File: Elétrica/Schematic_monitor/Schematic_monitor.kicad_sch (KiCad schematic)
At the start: 49 parts, among them J1 Conn_01x04, J2 USB_B_Micro, J3 Eletrode 1, J4 Eletrode 2, SW1 SW_Push, SW2 SW_SPDT, U1 STM32F446RET6TR, U2 LM1117S-3.3, U3 MLX90614ESF-ACC-000-TU, U4 MAX30100EFD+, U5 AD623, U6 LM358, U7 LM358, U8 LM358, Y1 Crystal_25MHz

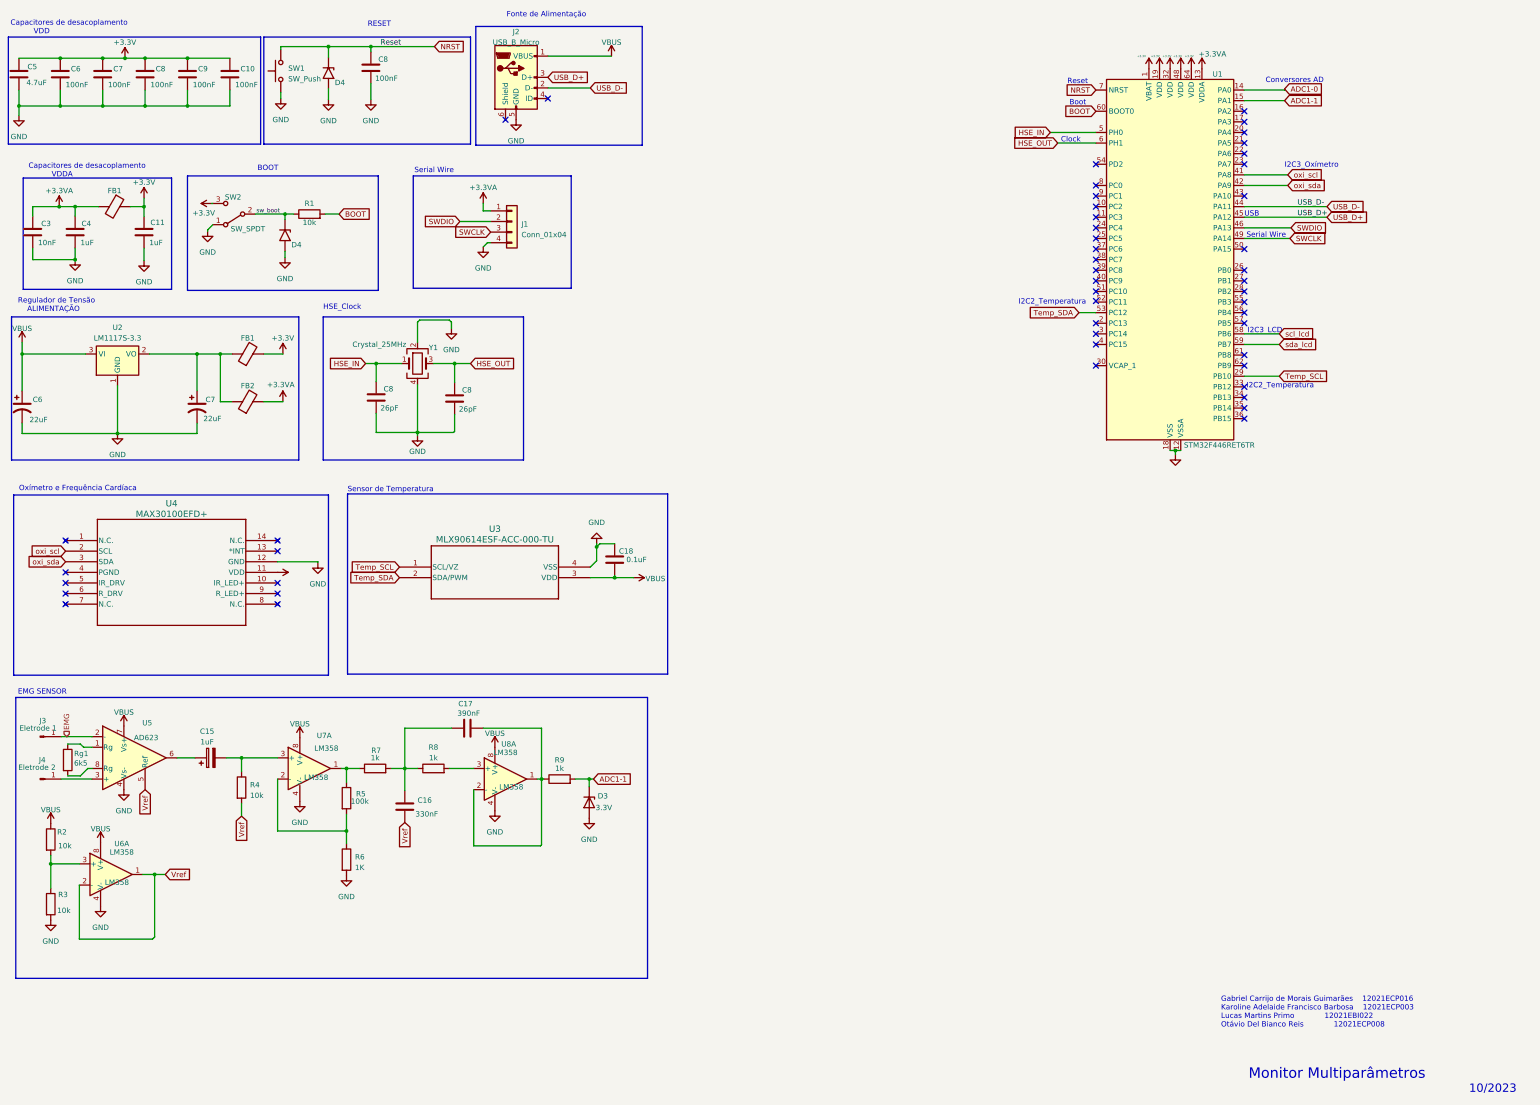
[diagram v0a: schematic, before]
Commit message: Versão PRJ2 e PRJ3 quase finalizada
Poucos detalhes precisam ser alterados para o envio dos trabalhos pelo menos do PRJ2. PRJ3 está finalizado
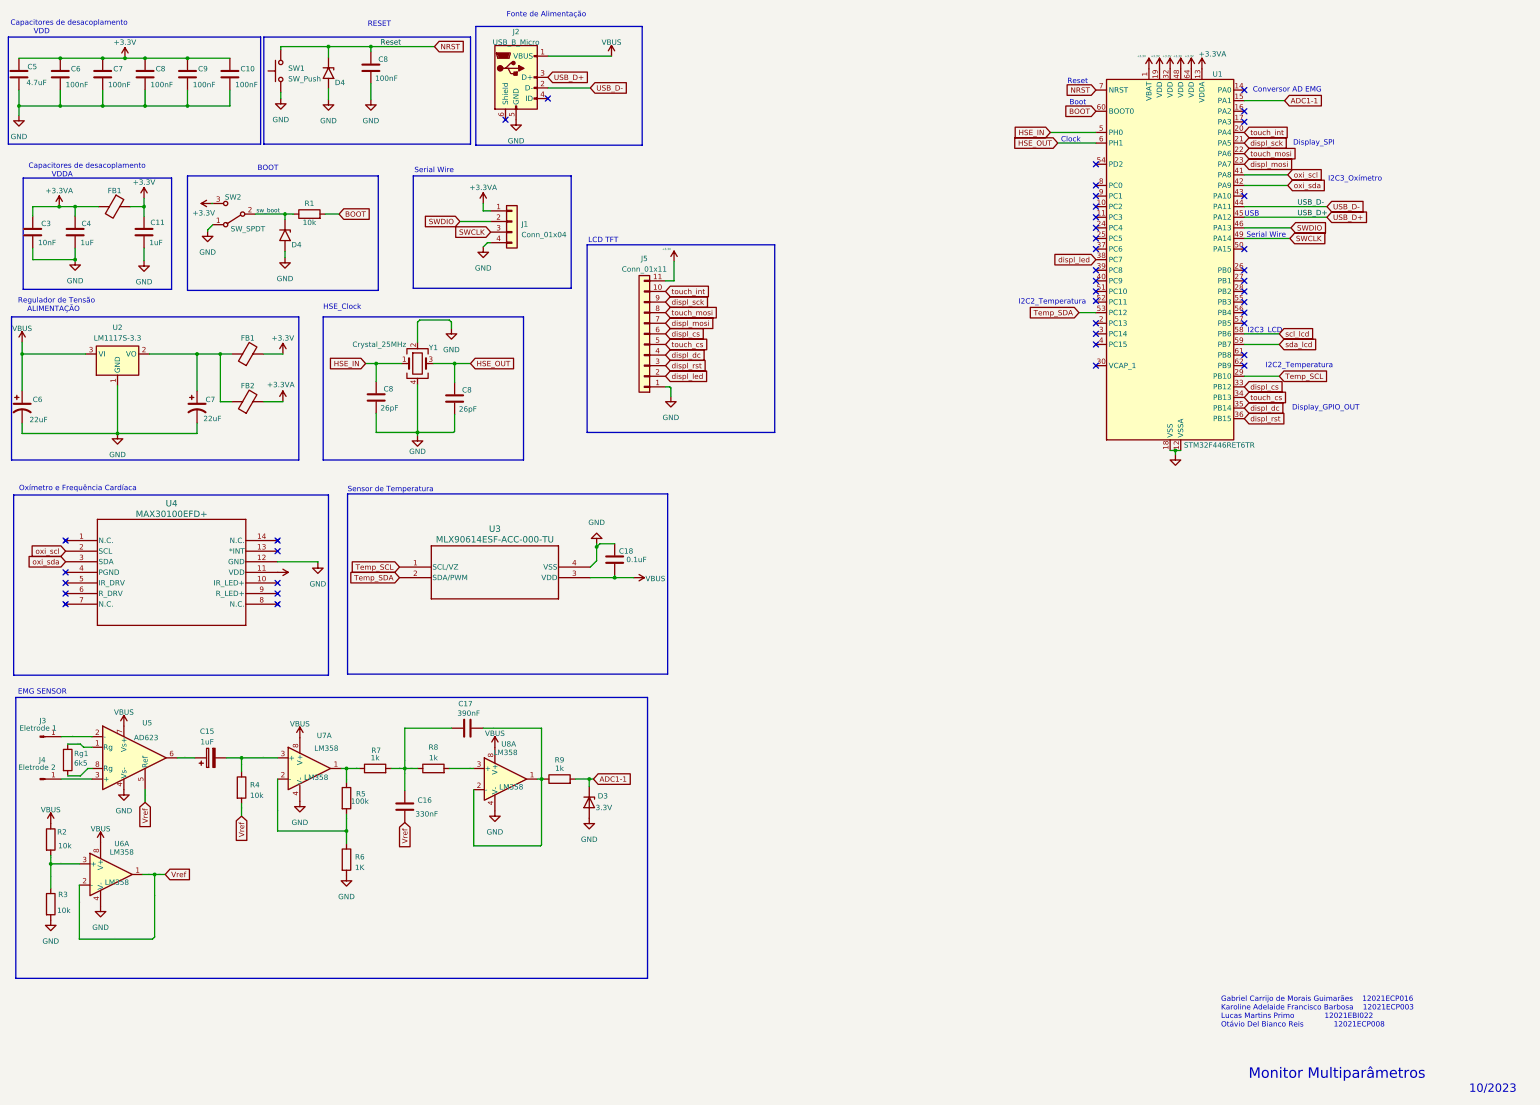
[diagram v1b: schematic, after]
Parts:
- added J5: Conn_01x11, Connector_PinSocket_1.00mm:PinSocket_1x11_P1.00mm_Vertical_SMD_Pin1Right, symbol Connector_Generic:Conn_01x11
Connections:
- net EMG is gone; now on net ADC1-1: J3.1 (Pin_1), U5.2 (-)
- net Vref is gone; now on net ADC1-1: C16.2, R4.2, U5.5 (Ref), U6.1, U6.2 (-)
- net +3.3V: now also J5.11 (Pin_11)
- net ADC1-1: now also C15.1, C15.2, C16.1, C17.1, C17.2, J4.1 (Pin_1), R2.2, R3.1, R4.1, R5.1, R5.2, R6.1, R7.1, R7.2, R8.1, R8.2, R9.1, Rg1.1, U5.1 (Rg), U5.3 (+), U5.6, U6.3 (+), U7.1, U7.2 (-), U7.3 (+), U8.1, U8.2 (-), U8.3 (+)
- net GND: now also J5.1 (Pin_1)
- net touch_int: now reaches U1.20 (PA4)
- net touch_int: now also J5.10 (Pin_10)
- net displ_sck: now reaches U1.21 (PA5)
- net displ_sck: now also J5.9 (Pin_9)
- net touch_mosi: now reaches U1.22 (PA6)
- net touch_mosi: now also J5.8 (Pin_8)
- net displ_mosi: now reaches U1.23 (PA7)
- net displ_mosi: now also J5.7 (Pin_7)
- net displ_cs: now reaches U1.33 (PB12)
- net displ_cs: now also J5.6 (Pin_6)
- net touch_cs: now reaches U1.34 (PB13)
- net touch_cs: now also J5.5 (Pin_5)
- net displ_dc: now reaches U1.35 (PB14)
- net displ_dc: now also J5.4 (Pin_4)
- net displ_rst: now reaches U1.36 (PB15)
- net displ_rst: now also J5.3 (Pin_3)
- net displ_led: now reaches U1.38 (PC7)
- net displ_led: now also J5.2 (Pin_2)
- net ADC1-0: no longer names the net of U1.14 (PA0)
- no-connect marks 49 -> 41
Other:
- note added: "Conversor AD EMG"
- note added: "Display_GPIO_OUT"
- note added: "Display_SPI"
- note added: "LCD TFT"
- note removed: "Conversores AD"

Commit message: Final Detalis to  PRJ2
Added final detalis in PCB desing and STM32 configuration.
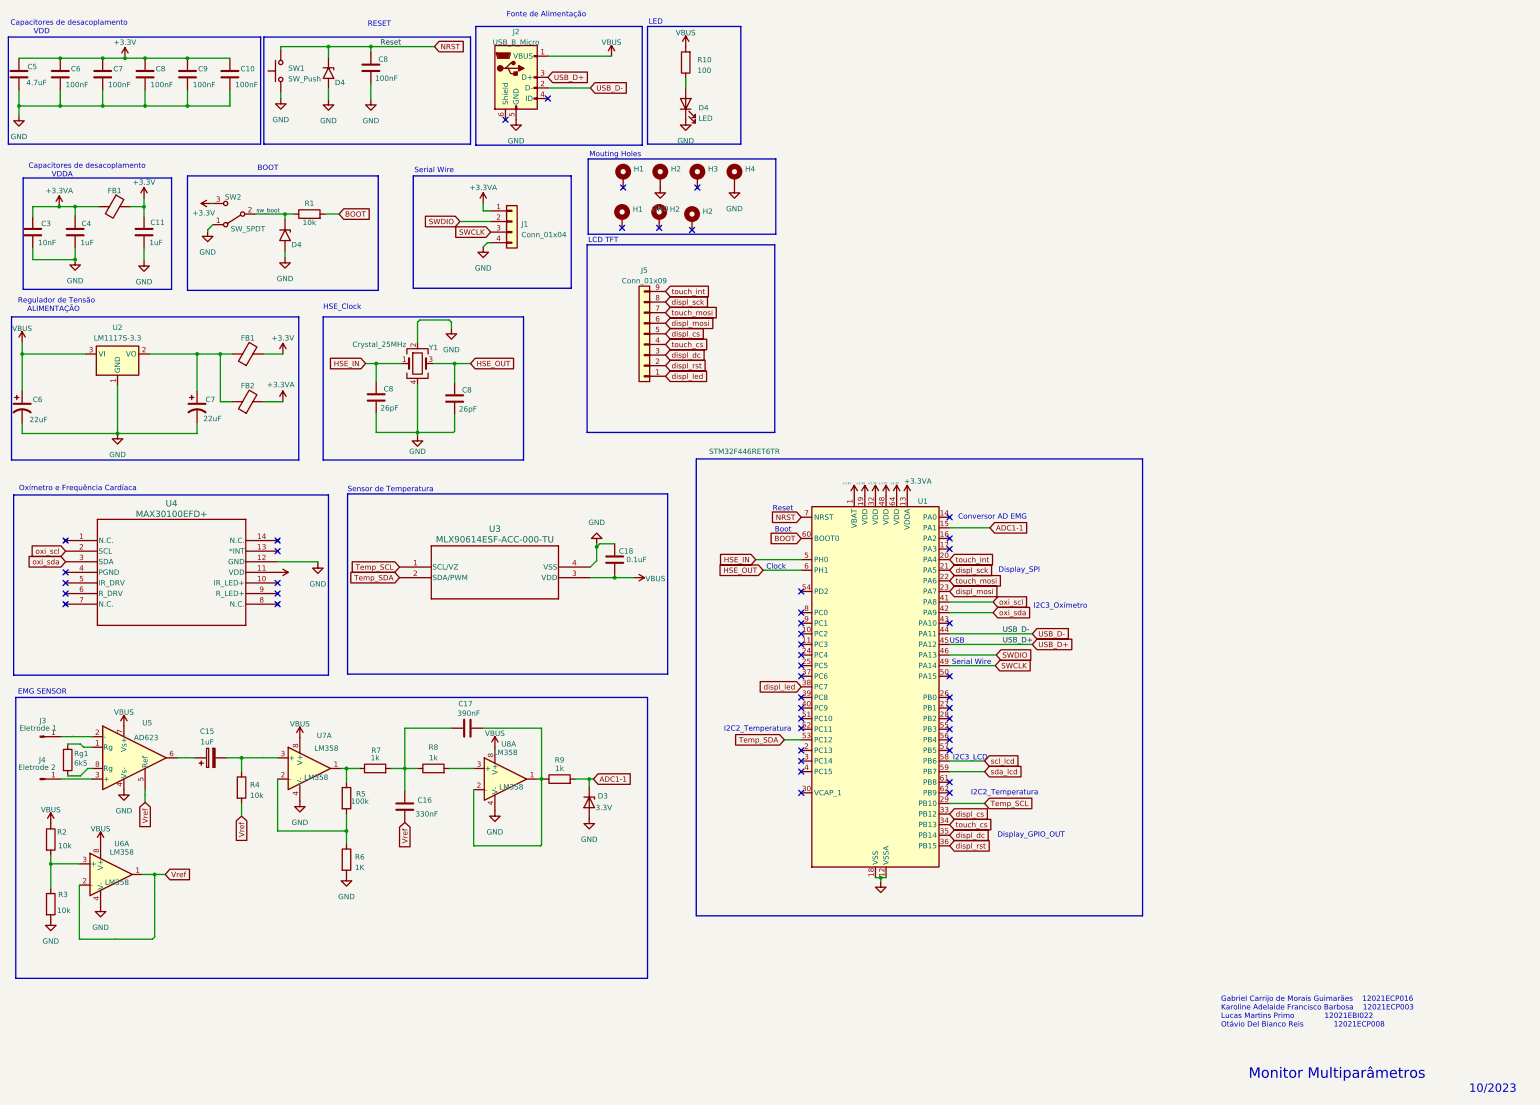
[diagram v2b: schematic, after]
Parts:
- removed J5: Conn_01x11, Connector_PinSocket_1.00mm:PinSocket_1x11_P1.00mm_Vertical_SMD_Pin1Right, symbol Connector_Generic:Conn_01x11
- added D4: LED, LED_SMD:LED_2010_5025Metric, symbol Device:LED
- added H1: ~, MountingHole:MountingHole_2.2mm_M2_DIN965_Pad, symbol Mechanical:MountingHole_Pad
- added H1, H2 (x3), H3, H4: MountingHole_Pad, MountingHole:MountingHole_2.2mm_M2_DIN965_Pad, symbol Mechanical:MountingHole_Pad
- added J5: Conn_01x09, Connector_PinSocket_2.54mm:PinSocket_1x09_P2.54mm_Vertical_SMD_Pin1Right, symbol Connector_Generic:Conn_01x09
- added R10: 100, Resistor_SMD:R_0805_2012Metric_Pad1.20x1.40mm_HandSolder, symbol Device:R
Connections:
- net GND: now also D4.1 (K), H2.1, H4.1
- net VBUS: now also R10.2
- net displ_cs: now also J5.5 (Pin_5)
- net displ_dc: now also J5.3 (Pin_3)
- net displ_led: now also J5.1 (Pin_1)
- net displ_mosi: now also J5.6 (Pin_6)
- net displ_rst: now also J5.2 (Pin_2)
- net displ_sck: now also J5.8 (Pin_8)
- net touch_cs: now also J5.4 (Pin_4)
- net touch_int: now also J5.9 (Pin_9)
- net touch_mosi: now also J5.7 (Pin_7)
- new net: D4.2 (A), R10.1
- no-connect marks 41 -> 46
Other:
- note added: "LED"
- note added: "Mouting Holes"
- moved on the sheet: U1
